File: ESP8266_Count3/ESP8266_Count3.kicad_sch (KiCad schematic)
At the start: 17 parts, among them J2 String1, J3 OLED, SW1 Test, U2 AMS1117-5.0, U2 WeMos_D1_mini, U4 74AHCT1G125, U4 INA219BxD

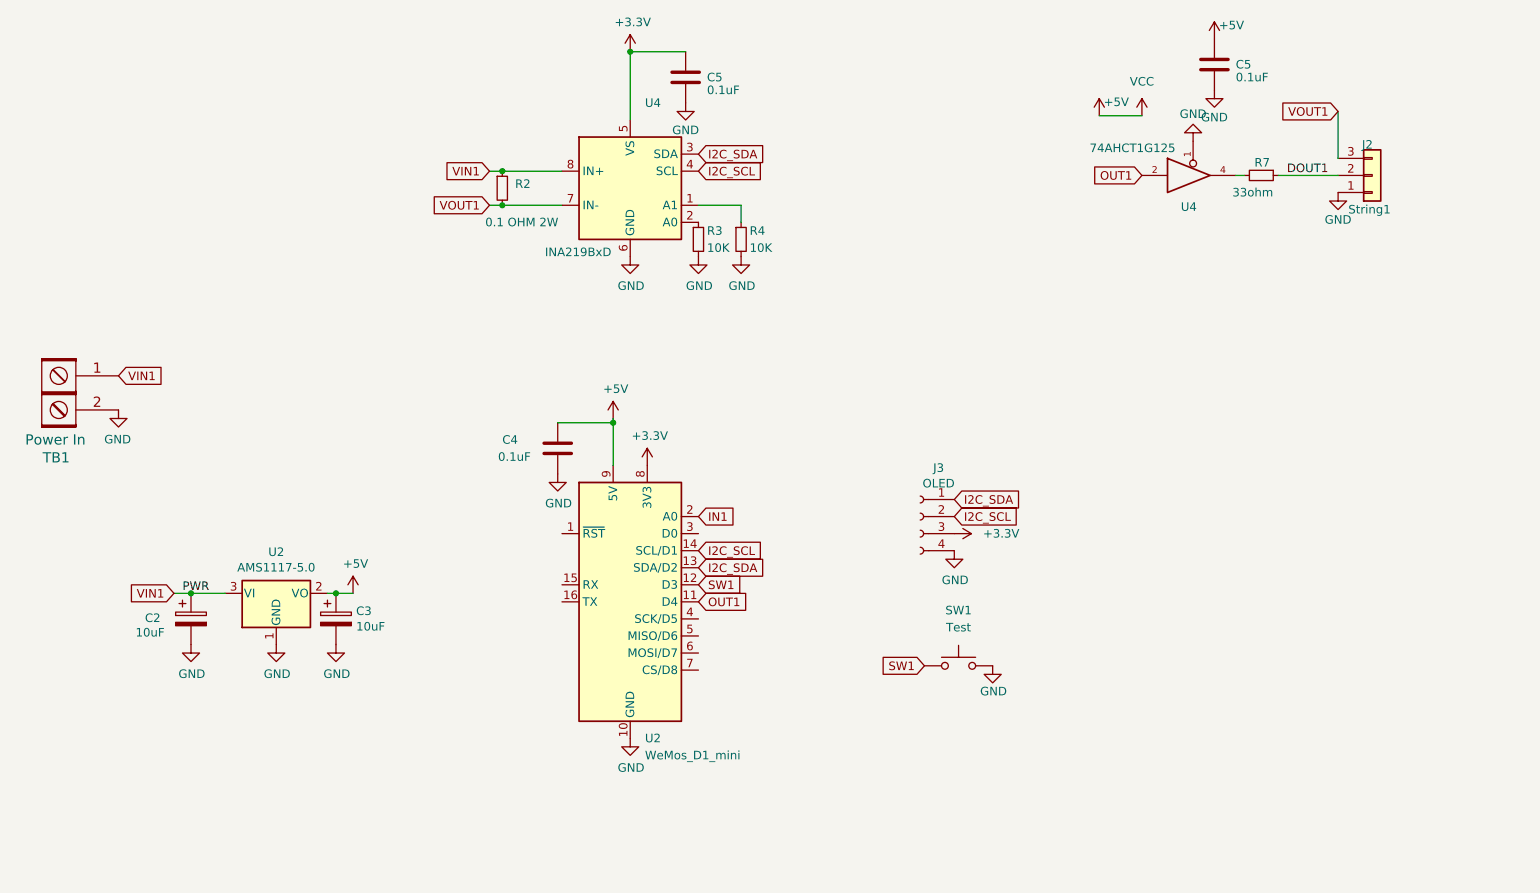
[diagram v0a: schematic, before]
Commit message: switch to RP2040
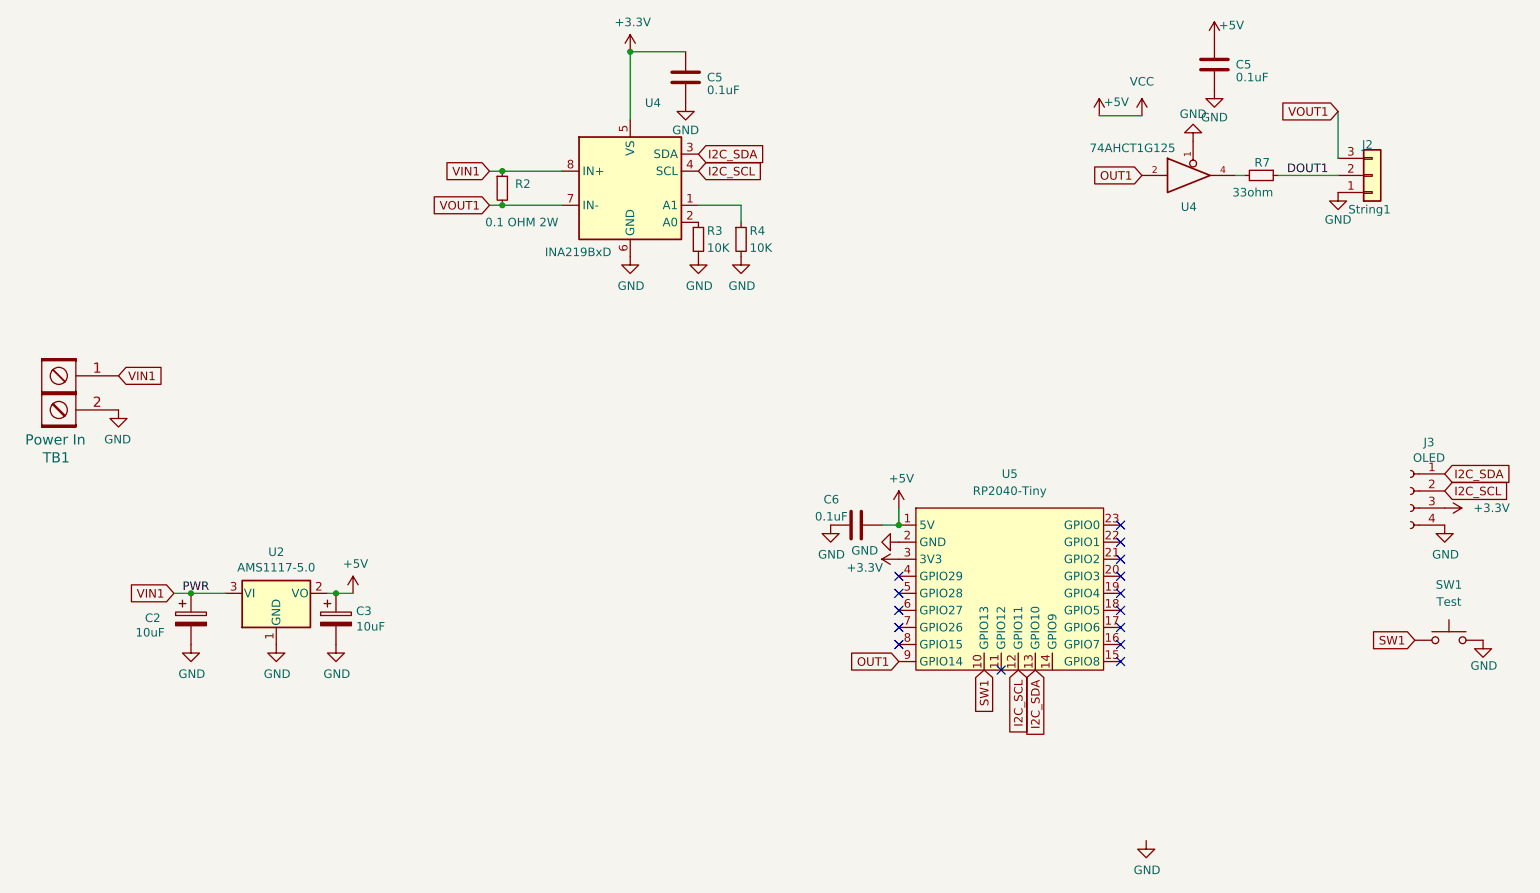
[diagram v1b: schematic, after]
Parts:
- removed C4: 0.1uF, Capacitor_SMD:C_0603_1608Metric_Pad1.08x0.95mm_HandSolder, symbol Device:C
- removed U2: WeMos_D1_mini, Module:WEMOS_D1_mini_light, symbol MCU_Module:WeMos_D1_mini
- added C6: 0.1uF, Capacitor_SMD:C_0603_1608Metric_Pad1.08x0.95mm_HandSolder, symbol Device:C
- added U5: RP2040-Tiny, Scotts:RP2040-Tiny_Scott, symbol RP2040-Tiny:RP2040-Tiny_Scott
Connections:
- net +3.3V: now also U5.3 (3V3)
- net +5V: now also C6.2, U5.1 (5V)
- net GND: now also C6.1, U5.2 (GND)
- net I2C_SCL: now also U5.12 (GPIO11)
- net I2C_SDA: now also U5.13 (GPIO10)
- net OUT1: now also U5.9 (GPIO14)
- net SW1: now also U5.10 (GPIO13)
- no-connect marks 0 -> 15
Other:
- title: (none) -> RP2040_Count
- moved on the sheet: J3, SW1
